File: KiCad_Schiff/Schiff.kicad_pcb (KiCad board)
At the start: 2 copper layers, 50 x 100 mm, 25 parts, among them J1 Conn_01x02, J3 Screw_Terminal_01x02, J4 Screw_Terminal_01x02, J5 L298N, J6 L298N, J7 AMS1117-Module, M1 Motor_Servo, M2 Motor_Servo, M3 Motor_Servo, SW1 SW_Wuerth_450301014042, SW2 SW_Wuerth_450301014042, U1 NRF24L01_Breakout, U2 TL072, U3 TL072

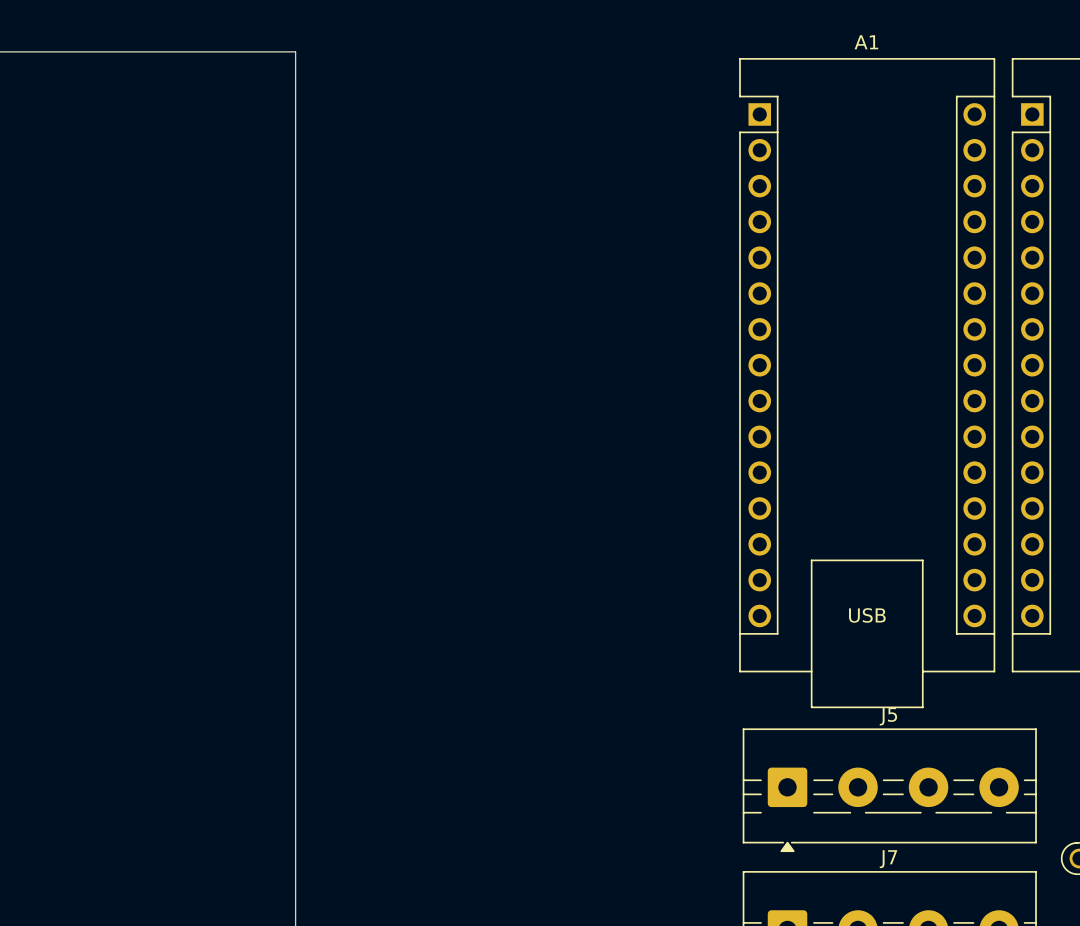
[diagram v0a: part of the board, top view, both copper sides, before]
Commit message: (Test)Code NRF-Modul
Test Code zum empfangen von Daten mit dem NRF-Modul (funktioniert)
Und aktualisierter Footprint der Arduinos in KiCad
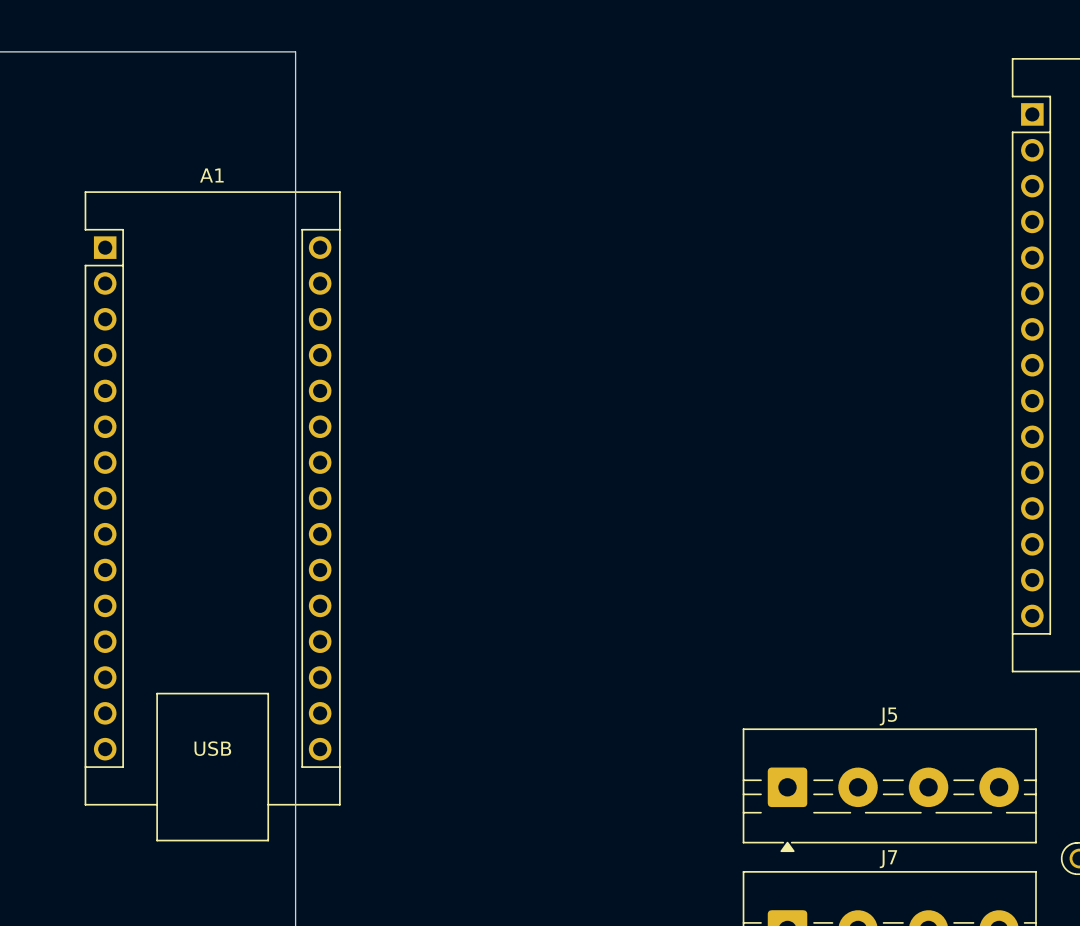
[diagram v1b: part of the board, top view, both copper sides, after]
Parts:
- moved A1 47.4 mm to (58.5, 35.4)
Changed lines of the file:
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@@
 	(footprint "Module:Arduino_Nano"
 		(layer "F.Cu")
-		(at 104.9095 25.935)
+		(at 58.5 35.38)
 		(descr "Arduino Nano, http://www.mouser.com/pdfdocs/Gravitech_Arduino_Nano3_0.pdf")
 		(tags "Arduino Nano")

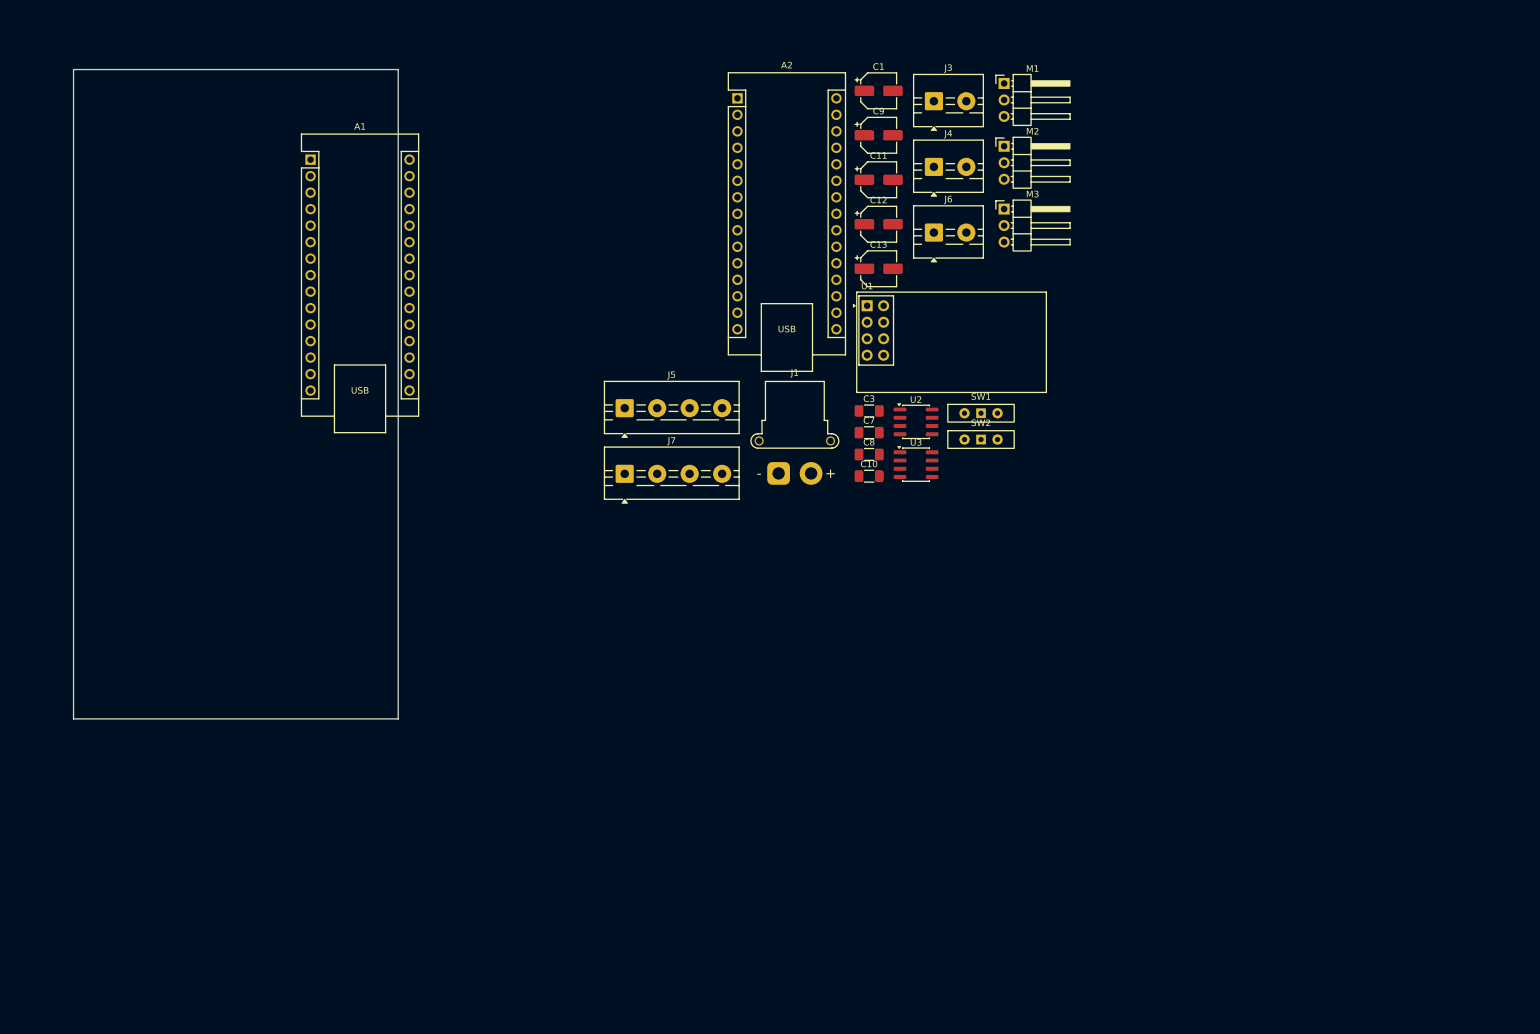
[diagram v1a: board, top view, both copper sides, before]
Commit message: New footprints for parts
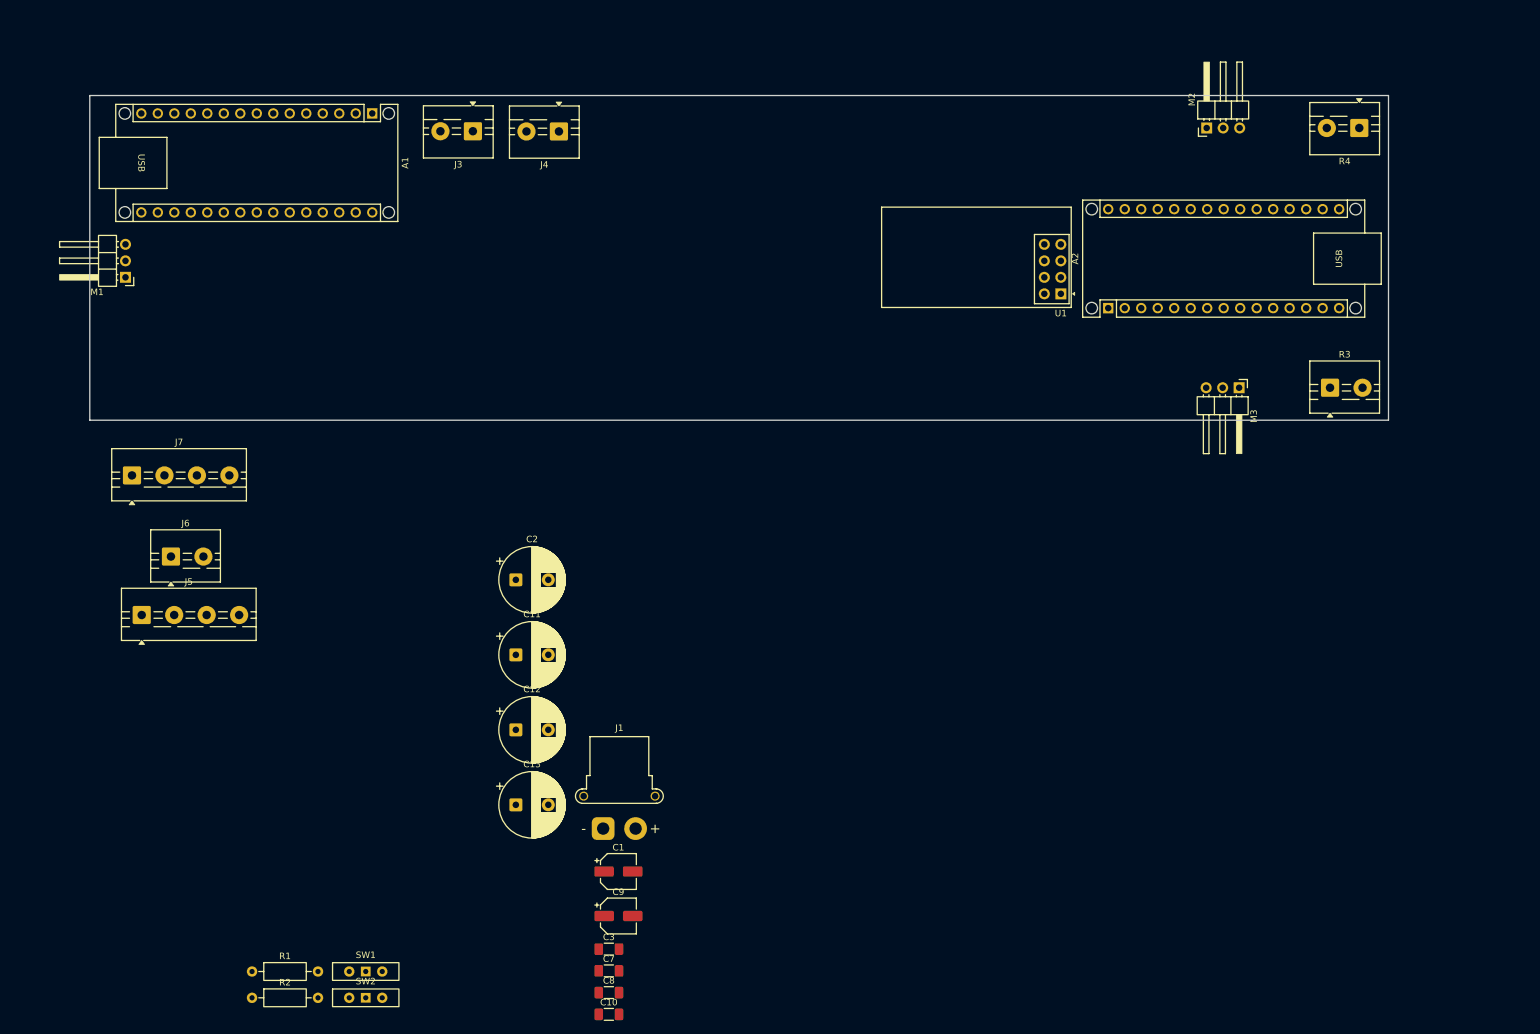
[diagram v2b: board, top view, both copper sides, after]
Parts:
- removed U2, U3: TL072, Package_SO:SOIC-8_3.9x4.9mm_P1.27mm
- added C2: 470u, Capacitor_THT:CP_Radial_D10.0mm_P5.00mm, F.Cu at (90.1, 100.1)
- added R1: R, Resistor_THT:R_Axial_DIN0207_L6.3mm_D2.5mm_P10.16mm_Horizontal, F.Cu at (49.5, 160.4)
- added R2: R, Resistor_THT:R_Axial_DIN0207_L6.3mm_D2.5mm_P10.16mm_Horizontal, F.Cu at (49.5, 164.4)
- added R3: R_Variable, TerminalBlock:TerminalBlock_MaiXu_MX126-5.0-02P_1x02_P5.00mm, F.Cu at (215.5, 70.5)
- added R4: R_Variable, TerminalBlock:TerminalBlock_MaiXu_MX126-5.0-02P_1x02_P5.00mm, F.Cu at (220.0, 30.5)
- A1, A2: footprint Module:Arduino_Nano -> Module:Arduino_Nano_WithMountingHoles
- C11, C12, C13: footprint Capacitor_SMD:CP_Elec_5x3 -> Capacitor_THT:CP_Radial_D10.0mm_P5.00mm
- C9: footprint Capacitor_SMD:CP_Elec_5x3 -> Capacitor_SMD:CP_Elec_5x4.4
- moved M1 138.6 mm to (30.0, 53.5), turned to 180 degrees
- moved SW1 127.9 mm to (67.0, 160.4)
- moved SW2 127.9 mm to (67.0, 164.4)
- moved J6 127.6 mm to (37.0, 96.5)
- moved C1 126.7 mm to (105.9, 145.0)
- moved C9 126.7 mm to (105.9, 151.8)
- moved C13 99.7 mm to (90.1, 134.7)
- moved C12 95.8 mm to (90.1, 123.2)
- moved C7 92.1 mm to (104.4, 160.3)
- moved C10 92.1 mm to (104.4, 167.0)
- moved C3 92.1 mm to (104.4, 156.9)
- moved C8 92.1 mm to (104.4, 163.7)
- moved C11 92.1 mm to (90.1, 111.6)
- moved J5 80.9 mm to (32.5, 105.5)
- moved J7 75.9 mm to (31.0, 84.0)
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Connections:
- A1 pad 13: unconnected-(A1-D10-Pad13) -> /Arduino_Com
- A1 pad 20: unconnected-(A1-A1-Pad20) -> Net-(A1-A1)
- A1 pad 21: unconnected-(A1-A2-Pad21) -> Net-(A1-A2)
- A1 pad 30: unconnected-(A1-VIN-Pad30) -> Net-(A1-VIN)
- A2 pad 10: Net-(A2-D7) -> unconnected-(A2-D7-Pad10)
- A2 pad 11: /ServoStear -> Net-(A2-D8)
- A2 pad 12: unconnected-(A2-D9-Pad12) -> /IN4
- A2 pad 13: unconnected-(A2-D10-Pad13) -> /Arduino_Com
- A2 pad 27: Net-(A2-+5V) -> unconnected-(A2-+5V-Pad27)
- A2 pad 30: unconnected-(A2-VIN-Pad30) -> Net-(A2-VIN)
- A2 pad 5: /IN1 -> /ServoStear
- A2 pad 6: /IN2 -> /IN1
- A2 pad 7: /IN3 -> unconnected-(A2-D4-Pad7)
- A2 pad 8: /IN4 -> /IN2
- A2 pad 9: Net-(A2-D6) -> /IN3
- C10 pad 2: Net-(A1-+5V) -> Net-(A1-VIN)
- C7 pad 2: Net-(A2-+5V) -> Net-(A2-VIN)
- J6 pad 2: VCC_BT -> +5V
- M1 pad 1: Net-(M1-PWM) -> /ServoStear
- M2 pad 1: Net-(M2-PWM) -> /ServoFoilL
- M3 pad 1: Net-(M3-PWM) -> /ServoFoilR
- SW1 pad 1: Net-(A1-+5V) -> Net-(A1-VIN)
- SW1 pad 3: +5V -> VCC_BT
- SW2 pad 1: Net-(A2-+5V) -> Net-(A2-VIN)
- SW2 pad 3: +5V -> VCC_BT
- U1 pad 3: Net-(A2-D6) -> unconnected-(U1-CE-Pad3)
- U1 pad 4: Net-(A2-D7) -> Net-(A2-D8)
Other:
- board size 50 x 100 mm -> 200 x 50 mm

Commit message: Begining of the layout
Unfinished layout of the Hydrofoil
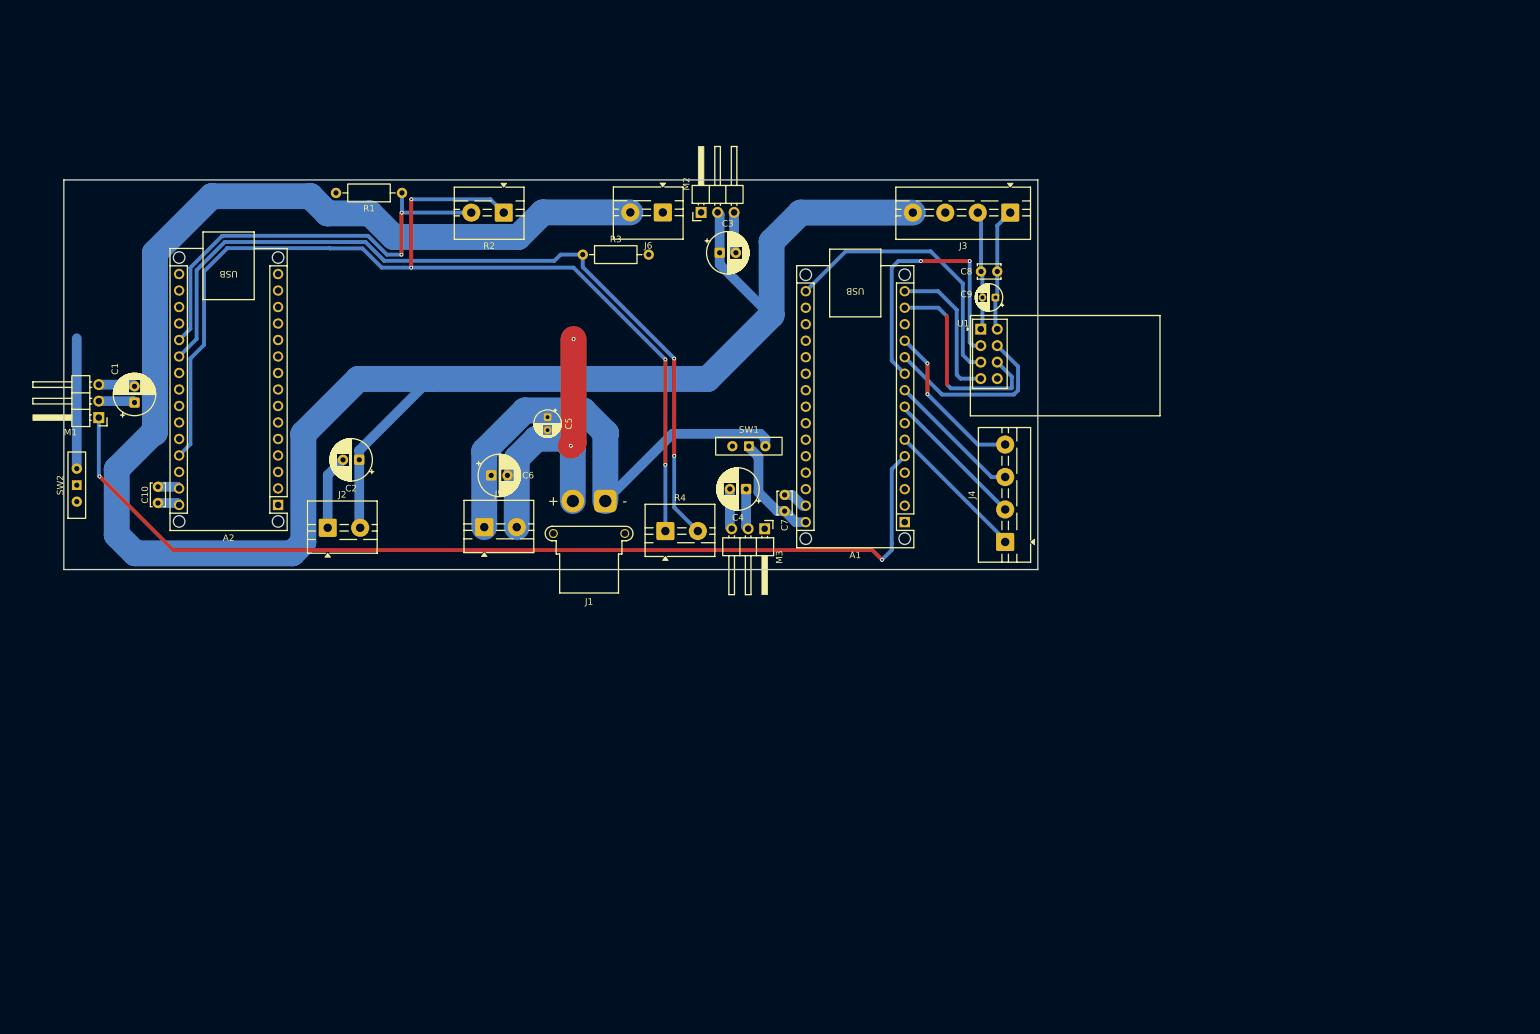
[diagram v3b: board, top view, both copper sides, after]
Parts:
- removed the C3 at (104.4, 156.9)
- added C2: 470u, Capacitor_THT:CP_Radial_D6.3mm_P2.50mm, F.Cu at (66.0, 81.6)
- C1: renamed from C11; footprint Capacitor_THT:CP_Radial_D10.0mm_P5.00mm -> Capacitor_THT:CP_Radial_D6.3mm_P2.50mm
- C10, C7, C8: footprint Capacitor_SMD:C_1206_3216Metric_Pad1.33x1.80mm_HandSolder -> Capacitor_THT:C_Disc_D3.4mm_W2.1mm_P2.50mm
- C3: renamed from C12; footprint Capacitor_THT:CP_Radial_D10.0mm_P5.00mm -> Capacitor_THT:CP_Radial_D6.3mm_P2.50mm
- C4: renamed from C13; footprint Capacitor_THT:CP_Radial_D10.0mm_P5.00mm -> Capacitor_THT:CP_Radial_D6.3mm_P2.50mm
- C5: renamed from C1; footprint Capacitor_SMD:CP_Elec_5x3 -> Capacitor_THT:CP_Radial_D4.0mm_P2.00mm
- C6: renamed from C2; footprint Capacitor_THT:CP_Radial_D10.0mm_P5.00mm -> Capacitor_THT:CP_Radial_D6.3mm_P2.50mm
- C9: footprint Capacitor_SMD:CP_Elec_5x4.4 -> Capacitor_THT:CP_Radial_D4.0mm_P2.00mm
- moved J3 141.2 mm to (166.2, 43.5), turned to 180 degrees
- moved J4 133.4 mm to (165.5, 94.2), turned to 90 degrees
- moved R2 132.4 mm to (88.2, 43.5)
- moved C8 126.1 mm to (164.2, 52.6), turned to 180 degrees
- moved R1 126.1 mm to (72.6, 40.5), turned to 180 degrees
- moved R3 121.6 mm to (100.4, 50.0)
- moved C9 111.6 mm to (164.0, 56.6), turned to 180 degrees
- moved C10 106.9 mm to (35.0, 85.8), turned to -90 degrees
- moved R4 104.7 mm to (113.1, 92.6)
- moved SW1 103.4 mm to (126.0, 79.5)
- moved SW2 87.1 mm to (22.5, 85.5), turned to 90 degrees
- moved C3 79.9 mm to (121.5, 49.7)
- moved M2 78.9 mm to (118.6, 43.5)
- moved C7 78.1 mm to (131.5, 87.0), turned to -90 degrees
- moved M3 76.2 mm to (128.4, 92.2)
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- renumbered A2 to A1, A1 to A2, J6 to J2, J7 to J3, J5 to J4, J3 to J5, J4 to J6, R2 to R1, R4 to R2, R1 to R3, R3 to R4, SW2 to SW1, SW1 to SW2
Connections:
- A1 pad 10: unconnected-(A2-D7-Pad10) (its old number) -> Net-(A1-D7)
- U1 pad 3: unconnected-(U1-CE-Pad3) -> Net-(A1-D7)
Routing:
- net +5V: track 0.00 -> 347.8 mm
- net Net-(A2-+5V): track 0.00 -> 161.6 mm, vias 0 -> 4
- net /ServoStear: track 0.00 -> 152.3 mm, vias 0 -> 2
- net Net-(A2-A2): track 0.00 -> 127.2 mm, vias 0 -> 2
- net GND: track 0.00 -> 101.1 mm, vias 0 -> 2
- net VCC_BT: track 0.00 -> 95.5 mm
- net Net-(A2-A1): track 0.00 -> 67.9 mm, vias 0 -> 2
- net Net-(A1-D7): track 0.00 -> 44.0 mm, vias 0 -> 2
- net Net-(A1-D13): track 0.00 -> 43.0 mm
- net Net-(A1-D11): track 0.00 -> 32.7 mm
- net Net-(A1-D8): track 0.00 -> 28.3 mm
- net /IN4: track 0.00 -> 24.9 mm, vias 0 -> 2
- net Net-(A1-D12): track 0.00 -> 23.1 mm
- net /IN2: track 0.00 -> 22.2 mm
- net /IN1: track 0.00 -> 22.2 mm
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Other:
- board size 200 x 50 mm -> 150 x 60 mm
